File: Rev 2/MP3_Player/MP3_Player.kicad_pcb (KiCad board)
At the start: 2 copper layers, 15.2 x 2.5 mm, 28 parts, among them J1 AudioJack3_SwitchT, M1 Haptic Feedback, Q1 BS170, SW1 Home, SW2 Back, SW3 Play/Pause, SW4 Power, SW5 Menu, SW6 Hold, U1 Wemos Lolin32 Lite

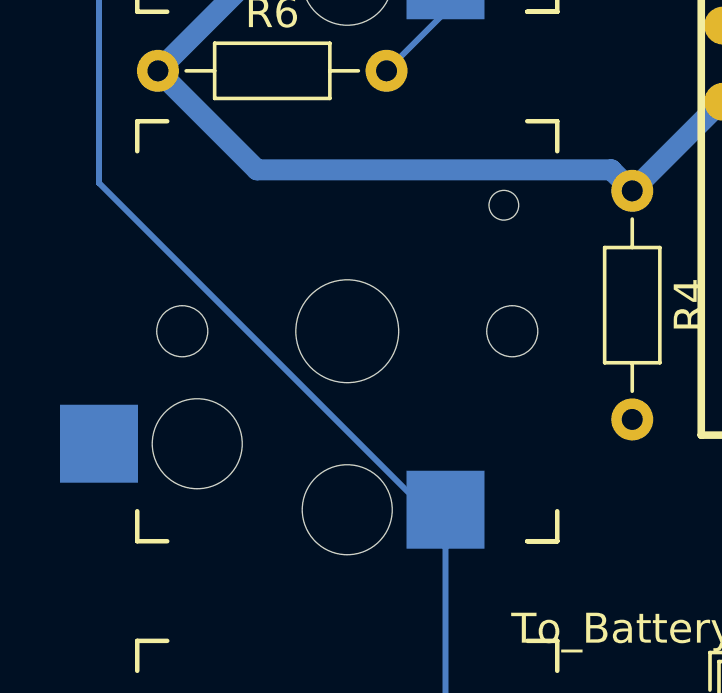
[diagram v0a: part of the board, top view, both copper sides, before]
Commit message: Imported ECE Shop DRC
-Imported DRC so we have the option open to print at the shop
-Fixed one trace that was close to a drill hole
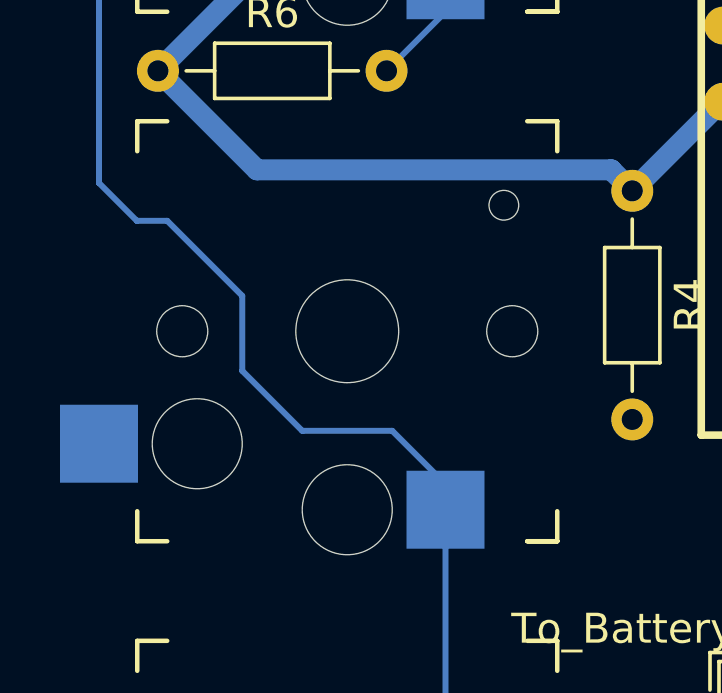
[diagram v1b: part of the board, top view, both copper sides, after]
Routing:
- net /VDD: track 253.6 -> 256.2 mm
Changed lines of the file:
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@@
 	)
 	(setup
+		(stackup
+			(layer "F.SilkS"
+				(type "Top Silk Screen")
+			)
+			(layer "F.Paste"
+				(type "Top Solder Paste")
+			)
+			(layer "F.Mask"
+				(type "Top Solder Mask")
+				(thickness 0.01)
+			)
+			(layer "F.Cu"
+				(type "copper")
+				(thickness 0.035)
+			)
+			(layer "dielectric 1"
+				(type "core")
+				(thickness 1.51)
+				(material "FR4")
+				(epsilon_r 4.5)
+				(loss_tangent 0.02)
+			)
+			(layer "B.Cu"
+				(type "copper")
+				(thickness 0.035)
+			)
+			(layer "B.Mask"
+				(type "Bottom Solder Mask")
+				(thickness 0.01)
+			)
+			(layer "B.Paste"
+				(type "Bottom Solder Paste")
+			)
+			(layer "B.SilkS"
+				(type "Bottom Silk Screen")
+			)
+			(copper_finish "None")
+			(dielectric_constraints no)
+		)
 		(pad_to_mask_clearance 0)
 		(allow_soldermask_bridges_in_footprints no)
@@
 	)
 	(segment
+		(start 98 112.5)
+		(end 95.5 110)
+		(width 0.2)
+		(layer "B.Cu")
+		(net 7)
+	)
+	(segment
 		(start 93.225 108.738705)
 		(end 93.225 99.78)
@@
 	)
 	(segment
+		(start 98 115)
+		(end 98 112.5)
+		(width 0.2)
+		(layer "B.Cu")
+		(net 7)
+	)
+	(segment
+		(start 94.486295 110)
+		(end 93.225 108.738705)
+		(width 0.2)
+		(layer "B.Cu")
+		(net 7)
+	)
+	(segment
 		(start 151 126)
 		(end 151 128)
@@
 	)
 	(segment
+		(start 104.775 119.63)
+		(end 104.5 119.355)
+		(width 0.2)
+		(layer "B.Cu")
+		(net 7)
+	)
+	(segment
 		(start 147 130.5)
 		(end 147 137)
@@
 	)
 	(segment
+		(start 95.5 110)
+		(end 94.486295 110)
+		(width 0.2)
+		(layer "B.Cu")
+		(net 7)
+	)
+	(segment
 		(start 174.25 119.5)
 		(end 163.9625 109.2125)
@@
 	)
 	(segment
-		(start 104.116295 119.63)
-		(end 93.225 108.738705)
-		(width 0.2)
-		(layer "B.Cu")
-		(net 7)
-	)
-	(segment
 		(start 104.775 119.63)
 		(end 104.775 136.95)
@@
 	)
 	(segment
+		(start 103 117)
+		(end 100 117)
+		(width 0.2)
+		(layer "B.Cu")
+		(net 7)
+	)
+	(segment
 		(start 104.775 119.63)
 		(end 104.116295 119.63)
@@
 	)
 	(segment
+		(start 100 117)
+		(end 98 115)
+		(width 0.2)
+		(layer "B.Cu")
+		(net 7)
+	)
+	(segment
 		(start 138.9495 75.5505)
 		(end 137.401877 75.5505)
@@
 		(layer "B.Cu")
 		(net 7)
+	)
+	(segment
+		(start 104.5 119.355)
+		(end 104.5 118.5)
+		(width 0.2)
+		(layer "B.Cu")
+		(net 7)
+	)
+	(segment
+		(start 104.5 118.5)
+		(end 103 117)
+		(width 0.2)
+		(layer "B.Cu")
+		(net 7)

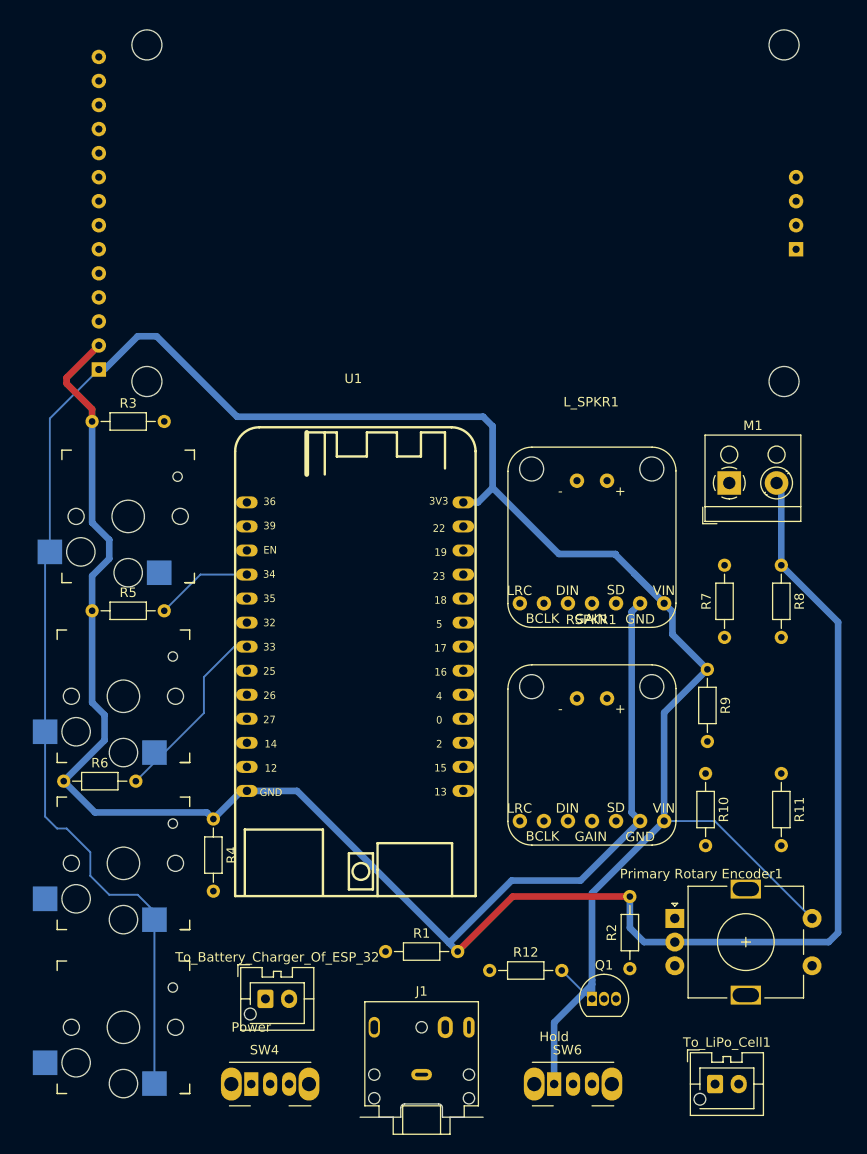
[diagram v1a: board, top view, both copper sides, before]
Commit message: Added Flyback Diode
-Added Flyback Diode to prevent sparking and unwanted behavior
-Finished high power rails
-Fixed Screen Orientation
-Fixed Placement of some components
-Fixed Silkscreen
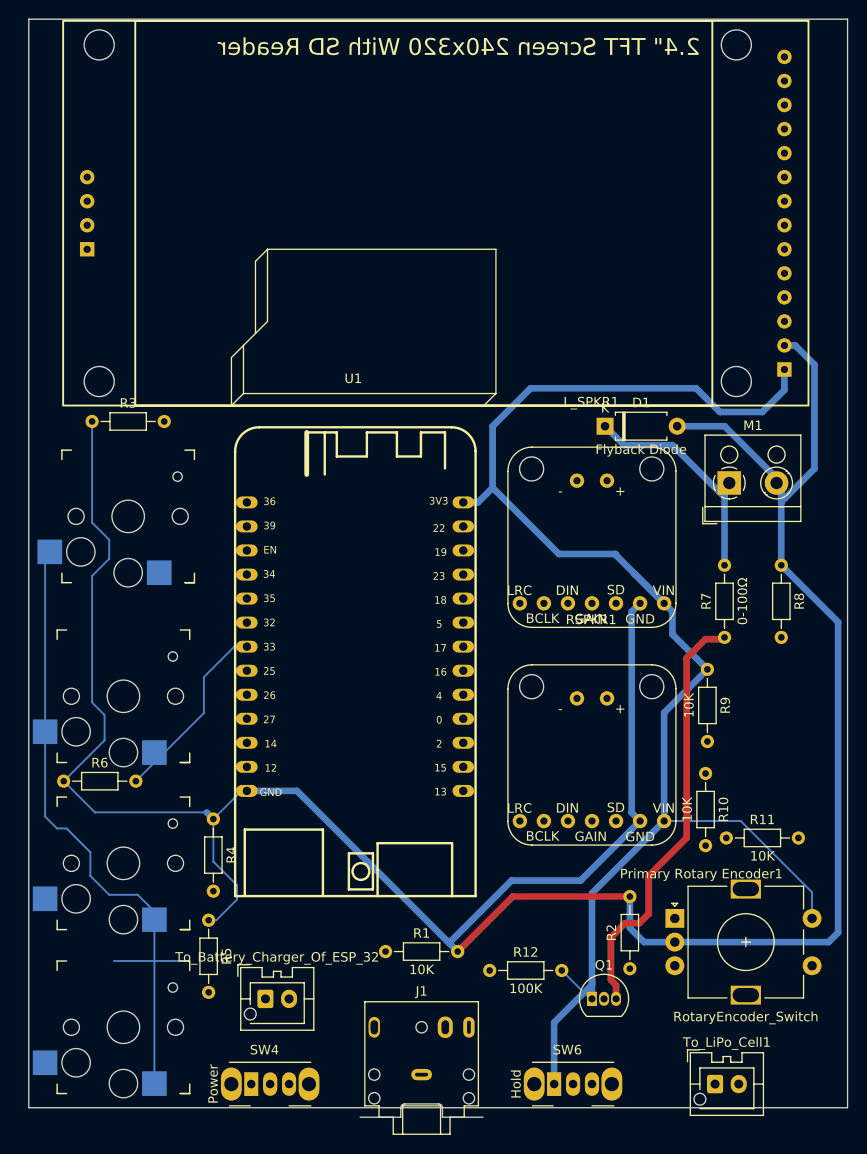
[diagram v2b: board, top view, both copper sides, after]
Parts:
- added D1: Flyback Diode, Diode_THT:D_A-405_P7.62mm_Horizontal, F.Cu at (152.4, 67.5)
- Screen&SDCardReader1: moved to B.Cu
- moved R5 34.9 mm to (110.5, 119.7), turned to -90 degrees
- moved R11 8.95 mm to (165.2, 111.0), turned to 0 degrees
- moved Screen&SDCardReader1 3.77 mm to (133.2, 45.0), turned to 180 degrees
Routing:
- net Net-(Q1-S): track 0.00 -> 45.3 mm
- net GND: track 250.9 -> 288.7 mm
- net Net-(D1-K): track 0.00 -> 24.6 mm
- net /VDD: track 256.2 -> 234.8 mm
- net Net-(SW5-B): track 10.3 -> 0.00 mm
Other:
- board size 15.2 x 2.5 mm -> 86.5 x 115 mm

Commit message: Almost finished routing traces
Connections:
- SW4 pad 2: Net-(SW4-B) -> +BATT
- To_Battery_Charger_Of_ESP_32 pad 1: Net-(SW4-B) -> +BATT
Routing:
- net /SPI_SCK: track 0.00 -> 183.7 mm
- net Net-(U1-IO0): track 0.00 -> 175.0 mm
- net /SPI_MISO: track 0.00 -> 123.3 mm
- net /SCREEN_BRIGHTNESS: track 0.00 -> 100.3 mm
- net -BATT: track 0.00 -> 90.5 mm
- net /SPI_MOSI: track 0.00 -> 82.1 mm
- net Net-(SW5-B): track 0.00 -> 78.9 mm
- net +BATT: track 0.00 -> 74.0 mm
- net Net-(RSPKR1-SPKR+): track 0.00 -> 73.6 mm
- net Net-(U1-IO27): track 0.00 -> 72.3 mm
- net /SD_CS: track 0.00 -> 68.0 mm
- net /RESET: track 0.00 -> 67.9 mm
- net Net-(SW3-B): track 0.00 -> 55.9 mm, vias 0 -> 1
- net Net-(L_SPKR1-SPKR-): track 0.00 -> 55.1 mm
- net /R_Chanel_Select: track 0.00 -> 54.9 mm
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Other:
- board size 86.5 x 115 mm -> 86.5 x 116 mm

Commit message: Finished routing PCB
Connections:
- SW4 pad 2: +BATT -> Net-(SW4-B)
- To_Battery_Charger_Of_ESP_32 pad 1: +BATT -> Net-(SW4-B)
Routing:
- net /Motor_Driver: track 0.00 -> 125.1 mm, vias 0 -> 2
- net Net-(U1-IO16): track 7.28 -> 114.1 mm
- net /TFT_DC: track 0.00 -> 95.4 mm
- net /TFT_CS: track 0.00 -> 80.9 mm
- net Net-(L_SPKR1-SPKR+): track 0.00 -> 73.6 mm, vias 0 -> 1
- net Net-(SW6-B): track 0.00 -> 65.4 mm, vias 0 -> 1
- net Net-(L_SPKR1-SPKR-): track 55.1 -> 111.8 mm, vias 0 -> 2
- net /Gain: track 25.6 -> 77.5 mm
- net /SPI_MOSI: track 82.1 -> 124.6 mm, vias 0 -> 1
- net /DAC_BCLK: track 39.4 -> 73.9 mm
- net Net-(RSPKR1-SPKR+): track 73.6 -> 49.1 mm, vias 0 -> 1
- net Net-(SW4-B): track 0.00 -> 9.80 mm
- net +BATT: track 74.0 -> 64.8 mm
- net /DAC_LRC: track 28.1 -> 34.8 mm
- net /SPI_SCK: track 183.7 -> 181.8 mm
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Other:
- board size 86.5 x 116 mm -> 87.5 x 116 mm
